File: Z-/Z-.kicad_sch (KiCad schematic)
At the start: 21 parts, among them J1 200528-0100, J2 Conn_Coaxial, J3 Conn_Coaxial, J4 200528-0100, J5 Conn_01x02

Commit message: Z- Board Files
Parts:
- AE3: value GPS Antenna -> CGGBP.18.4.A.02; Field5 (none) -> GPS Antenna
- BA1: value ATB2012-50011-T000 -> DXW21HN5011BL
- J2, J3: value Conn_Coaxial -> U.FL
- J5: symbol Connector_Generic:Conn_01x02 -> Connector_Generic_MountingPin:Conn_01x02_MountingPin
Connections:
- net BURN_EN1: now also J4.8 (Pin_8); no longer J4.3 (Pin_3)
- net BURN_EN2: now also J4.7 (Pin_7); no longer J4.4 (Pin_4)
- net BURN_EN3: now also J4.6 (Pin_6); no longer J4.5 (Pin_5)
- net BURN_EN4: now also J4.5 (Pin_5); no longer J4.6 (Pin_6)
- net BURN_RELAY_A: now also J4.9 (Pin_9); no longer J4.2 (Pin_2)
- net GND: now also J4.2 (Pin_2), J4.3 (Pin_3), J4.4 (Pin_4), J5.MP (MountPin); no longer J4.7 (Pin_7), J4.8 (Pin_8), J4.9 (Pin_9)
- net VBATT: no longer J1.10 (Pin_10), J1.8 (Pin_8), J1.9 (Pin_9)
- new net VBATT_SENSE: J1.10 (Pin_10), J1.8 (Pin_8), J1.9 (Pin_9)

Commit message: Z- Solar Panel files upload
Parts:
- added U6: PCA9685BS, Package_DFN_QFN:QFN-28-1EP_6x6mm_P0.65mm_EP4.25x4.25mm, symbol Driver_LED:PCA9685BS
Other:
- moved on the sheet: AE1, AE2, AE3, BA1, J2, J3, J4

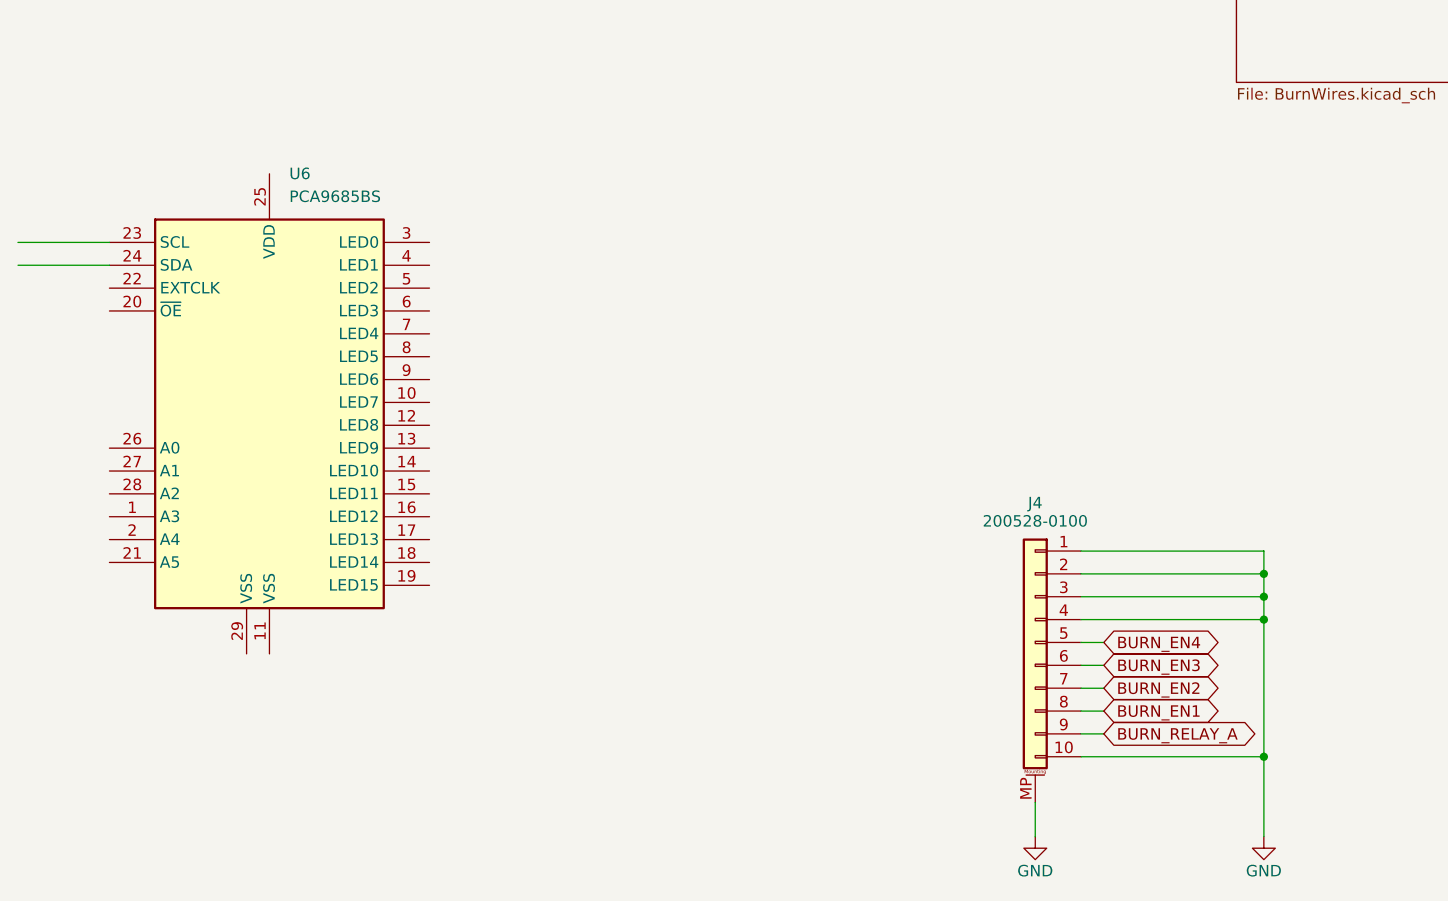
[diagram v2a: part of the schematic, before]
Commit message: Added i2c expander for burnwires, reformatted i2c protection, swapped to drv8235
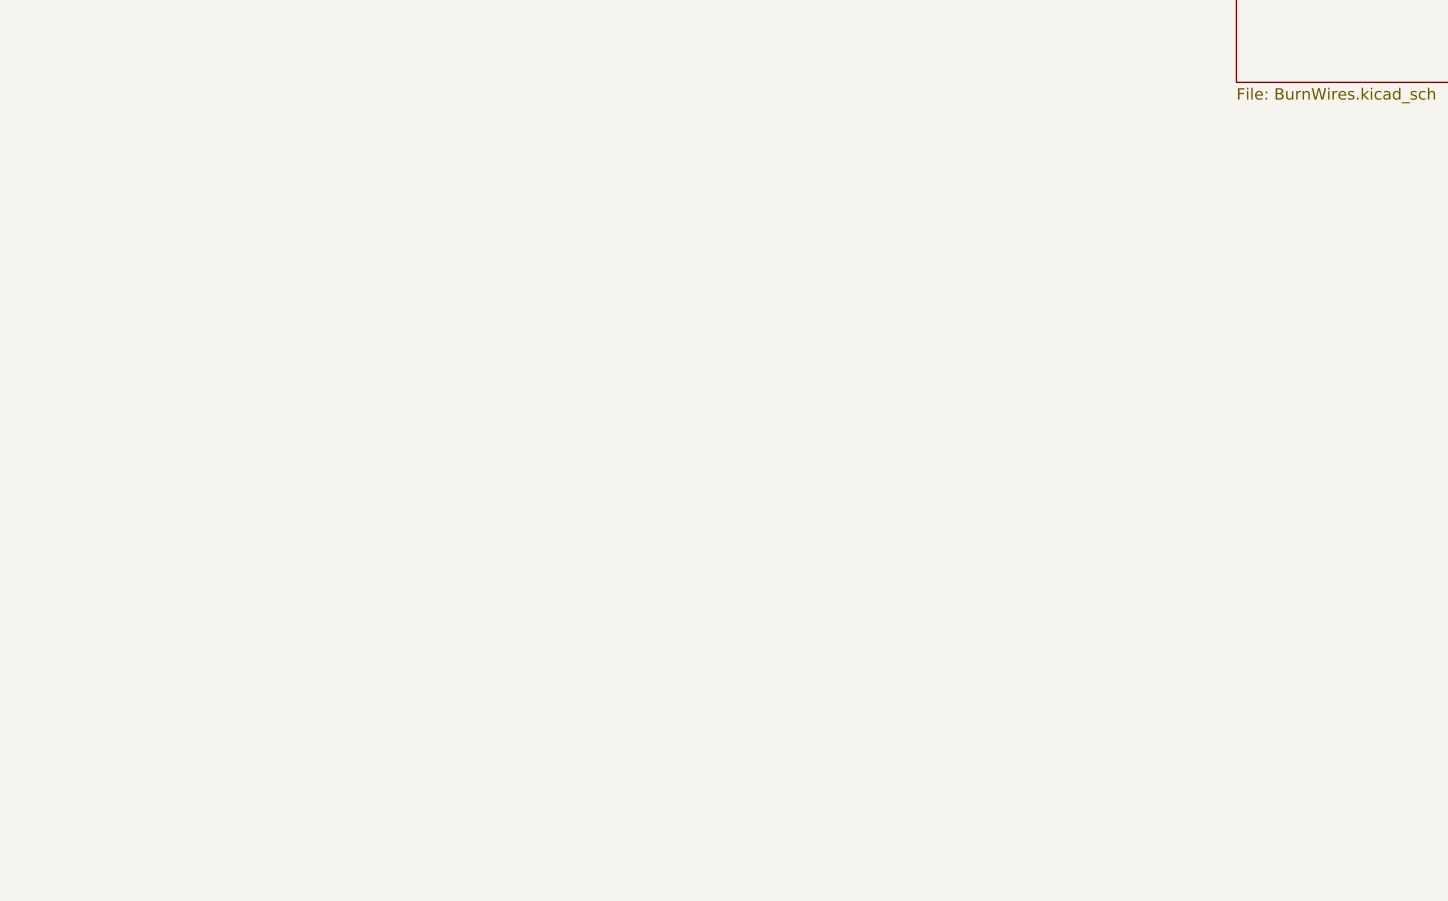
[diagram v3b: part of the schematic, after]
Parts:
- removed J4: 200528-0100, Connector_FFC-FPC:Molex_200528-0100_1x10-1MP_P1.00mm_Horizontal, symbol SolarPanels:Conn_01x10_MountingPin
- removed U6: PCA9685BS, Package_DFN_QFN:QFN-28-1EP_6x6mm_P0.65mm_EP4.25x4.25mm, symbol Driver_LED:PCA9685BS

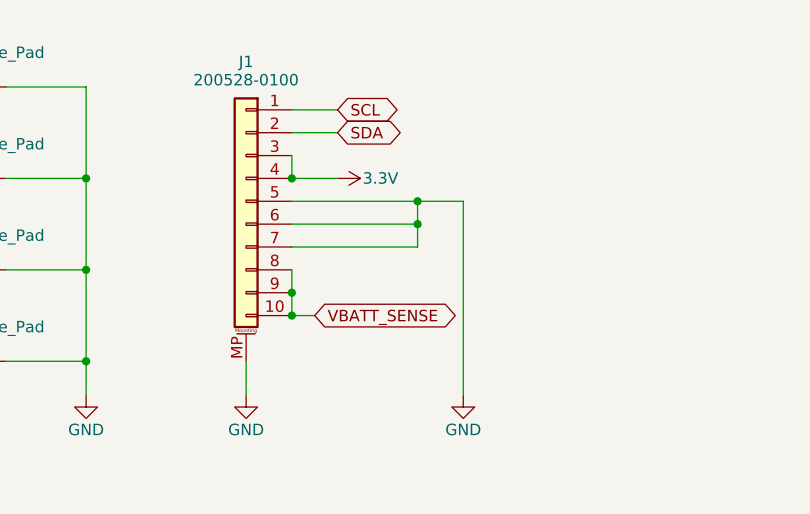
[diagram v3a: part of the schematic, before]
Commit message: Moved burnwire around and added switch to coil driver
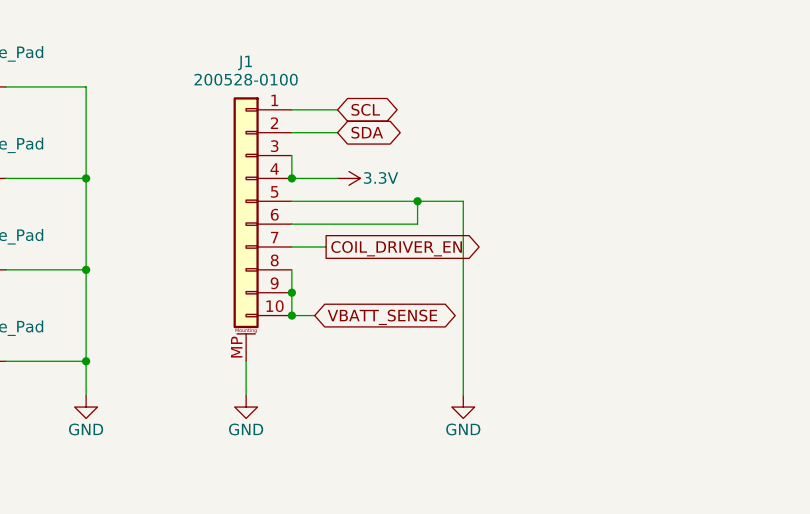
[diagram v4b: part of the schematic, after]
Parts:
- AE1, AE2: footprint SolarPanels:Antenna Mount -> Argus-Miscellaneous:Antenna Mount; symbol SolarPanels:MountingHole_Pad -> Mechanical:MountingHole_Pad
- AE3: footprint SolarPanels:ANT_CGGBP.18.4.A.02_TAL -> Argus-Miscellaneous:ANT_CGGBP.18.4.A.02_TAL; symbol SolarPanels:Antenna -> Argus-Passives:Antenna
- BA1: footprint SolarPanels:ATB2012 -> Argus-Passives:ATB2012; symbol SolarPanels:ATB2012 -> Argus-Passives:ATB2012
- H1, H2, H3, H4, H5, H6, H7, H8: footprint SolarPanels:MountingHole_3.2mm_M3_DIN965_Pad_TopBottom -> Argus-Miscellaneous:MountingHole_3.2mm_M3_DIN965_Pad_TopBottom; symbol SolarPanels:MountingHole_Pad -> Mechanical:MountingHole_Pad
- J1: symbol SolarPanels:Conn_01x10_MountingPin -> Connector_Generic_MountingPin:Conn_01x10_MountingPin
- J2, J3: symbol SolarPanels:Conn_Coaxial -> Connector:Conn_Coaxial
- R6, R7, R8, R9: symbol SolarPanels:R_Small -> Device:R_Small
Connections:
- net GND: no longer J1.7 (Pin_7)
- new net COIL_DRIVER_EN: J1.7 (Pin_7)

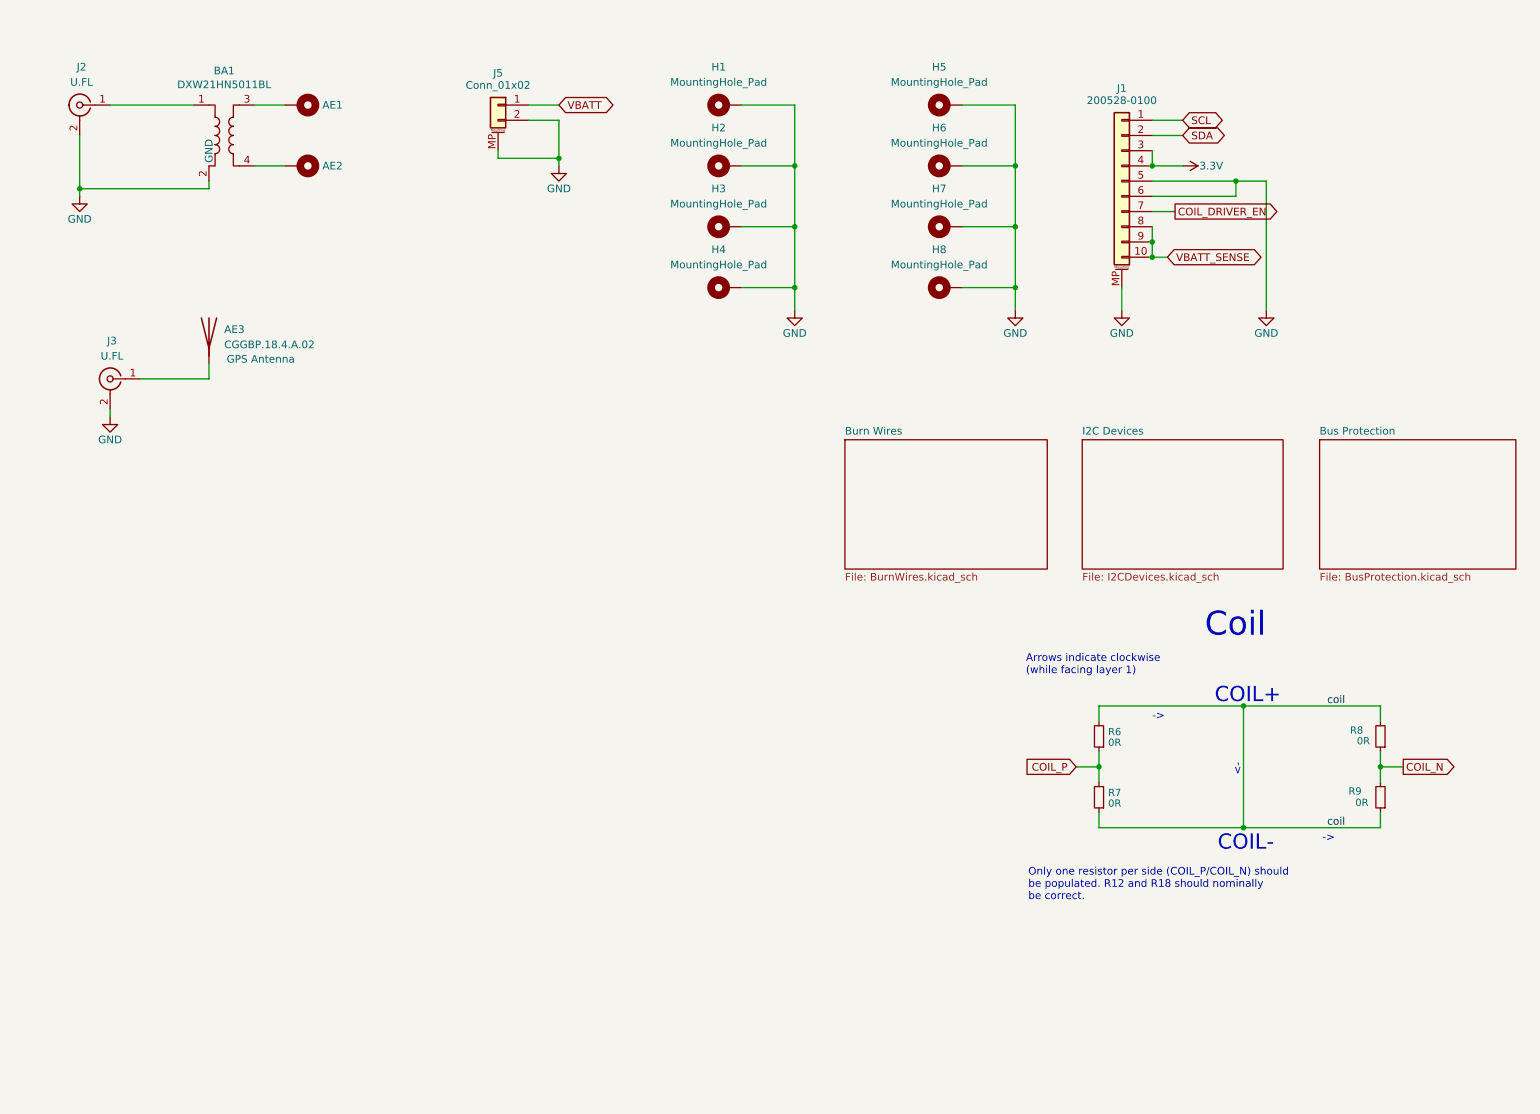
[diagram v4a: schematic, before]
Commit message: Started adding main/peripheral 3v3 nets
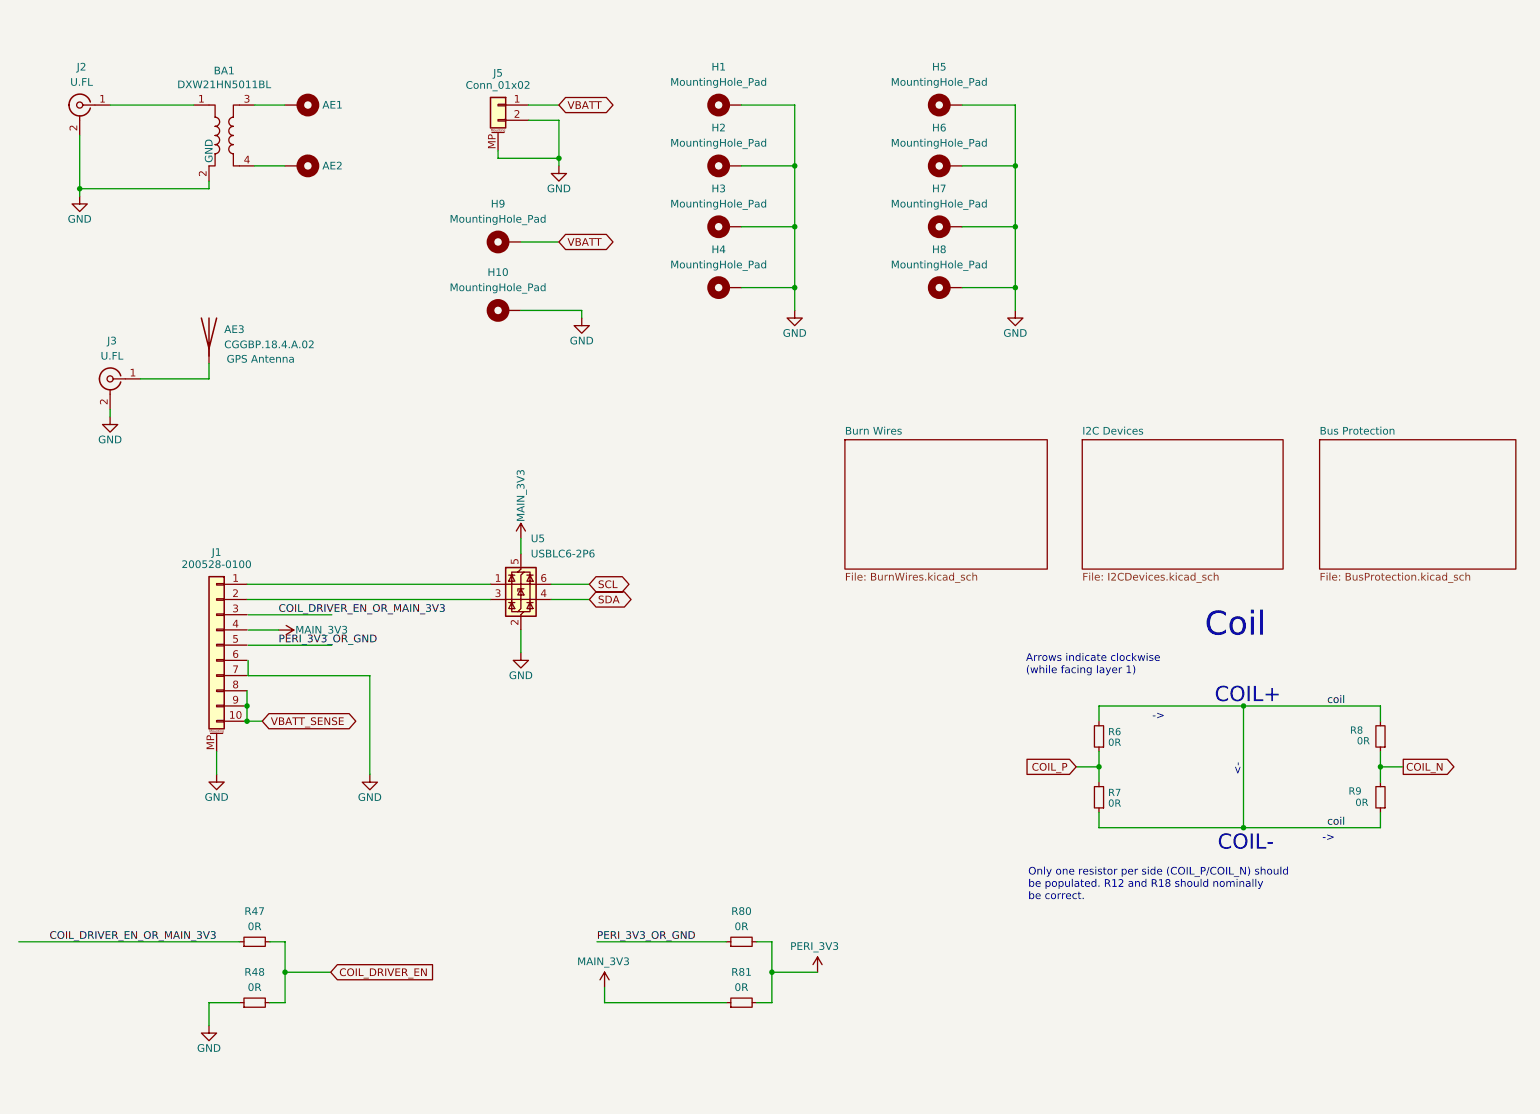
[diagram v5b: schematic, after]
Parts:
- added H10, H9: MountingHole_Pad, Argus-Connectors:20AWG Through Hole, symbol Mechanical:MountingHole_Pad
- added R47, R48, R80, R81: 0R, Resistor_SMD:R_0603_1608Metric, symbol Device:R_Small
- added U5: USBLC6-2P6, Package_TO_SOT_SMD:SOT-666, symbol Power_Protection:USBLC6-2P6
- J1: footprint Connector_FFC-FPC:Molex_200528-0100_1x10-1MP_P1.00mm_Horizontal -> Argus-Connectors:Molex_200528-0100_1x10-1MP_P1.00mm_Horizontal
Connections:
- net COIL_DRIVER_EN: now also R47.2, R48.2; no longer J1.7 (Pin_7)
- net GND: now also H10.1, R48.1, U5.2 (GND); no longer J1.5 (Pin_5), J1.6 (Pin_6)
- net SCL: now also U5.6 (I/O1); no longer J1.1 (Pin_1)
- net SDA: now also U5.4 (I/O2); no longer J1.2 (Pin_2)
- net VBATT: now also H9.1
- net 3.3V: no longer names the net of J1.3 (Pin_3)
- net 3.3V: no longer J1.4 (Pin_4)
- new net: J1.1 (Pin_1), U5.1 (I/O1)
- new net: J1.2 (Pin_2), U5.3 (I/O2)
- new net COIL_DRIVER_EN_OR_MAIN_3V3: R47.1
- new net MAIN_3V3: R81.1, U5.5 (VBUS)
- new net PERI_3V3: R80.2, R81.2
- new net PERI_3V3_OR_GND: R80.1
